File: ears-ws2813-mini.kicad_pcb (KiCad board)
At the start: 2 copper layers, 113 x 153 mm, 204 parts, among them J1 Conn_01x08, J2 Conn_01x02, J3 Conn_01x02, J4 Conn_01x02, J5 Conn_01x02

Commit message: Hopefully this will be revision 2.0
Signed-off-by: Aaron Williams <aaron.w2@gmail.com>
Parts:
- added C100: 4.7nF, Capacitor_SMD:C_0603_1608Metric, F.Cu at (62.4, 185.8)
- added C101: 4.7nF DNI, Capacitor_SMD:C_0603_1608Metric, F.Cu at (69.9, 168.2)
- added C102: 4.7nF DNI, Capacitor_SMD:C_0603_1608Metric, F.Cu at (35.5, 167.0)
- added C99: 4.7nF, Capacitor_SMD:C_0603_1608Metric, F.Cu at (64.0, 185.8)
- C10, C11, C12, C13, C14, C15, C16, C17, C18, C19, C20, C21, C22, C23, C24, C25, C26, C27, C28, C29, C3, C30, C31, C32, C33, C34, C35, C36, C37, C38, C39, C4, C40, C41, C42, C43, C44, C45, C46, C47, C48, C49, C5, C50, C51, C52, C53, C54, C55, C56, C57, C58, C59, C6, C60, C61, C62, C63, C64, C65, C66, C67, C68, C69, C7, C70, C71, C72, C73, C74, C75, C76, C77, C78, C79, C8, C80, C81, C82, C83, C84, C85, C86, C87, C88, C89, C9, C90, C91, C92, C93, C94, C95, C96, C97, C98: value 1uF -> 1uF 25V
- D1, D10, D11, D12, D13, D14, D15, D16, D17, D18, D19, D2, D20, D21, D22, D23, D24, D25, D26, D27, D28, D29, D3, D30, D31, D32, D33, D34, D35, D36, D37, D38, D39, D4, D40, D41, D42, D43, D44, D45, D46, D47, D48, D49, D5, D50, D51, D52, D53, D54, D55, D56, D57, D58, D59, D6, D60, D61, D62, D63, D64, D65, D66, D67, D68, D69, D7, D70, D71, D72, D73, D74, D75, D76, D77, D78, D79, D8, D80, D81, D82, D83, D84, D85, D86, D87, D88, D89, D9, D90, D91, D92, D93, D94, D95, D96: footprint LED_WS2813-mini:LED_WS2813-MINI -> LED_WS2813-mini:LED_WS2813-MINI-2
- moved R2 39.3 mm to (28.5, 167.0), turned to 0 degrees
- moved R1 18.5 mm to (63.4, 168.1), turned to 0 degrees
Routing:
- net Net-(C100-Pad1): track 5.99 -> 73.0 mm, vias 0 -> 3
- net /DIN: track 75.6 -> 15.5 mm
- net Net-(C101-Pad1): track 3.21 -> 29.4 mm
- net /DINB: track 73.3 -> 49.1 mm, vias 0 -> 1
- net GND: track 236.7 -> 253.0 mm, vias 193 -> 196
- net +5V: track 262.4 -> 269.4 mm, vias 21 -> 19
- net /Ears-top and bypass/DOUT7: track 73.1 -> 78.6 mm
- net /Ears-top and bypass/DOUT6: track 80.5 -> 85.4 mm
- net /DOUT1: track 123.2 -> 128.0 mm, vias 4 -> 5
- net /DOUT4: track 102.8 -> 107.3 mm
- net Net-(D50-Pad3): track 13.5 -> 17.1 mm, vias 4 -> 2
- net /DOUT2: track 115.7 -> 119.2 mm, vias 4 -> 5
- net Net-(D82-Pad3): track 13.8 -> 17.2 mm, vias 4 -> 2
- net /DOUT3: track 109.2 -> 112.4 mm, vias 4 -> 5
- net Net-(D37-Pad3): track 14.2 -> 17.4 mm, vias 4 -> 2
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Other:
- board text added: "+ + - -"
- board text added: "+5 GND"
- board text added: "Copyright © 2019 by Aaron Williams"
- board text added: "DIB DI DO DOB"
- board text added: "DIB DI DO DOB 5 5 G G"
- board text added: "DO DOB"
- board text added: "DOB DO"
- board text added: "Revision 2.0"

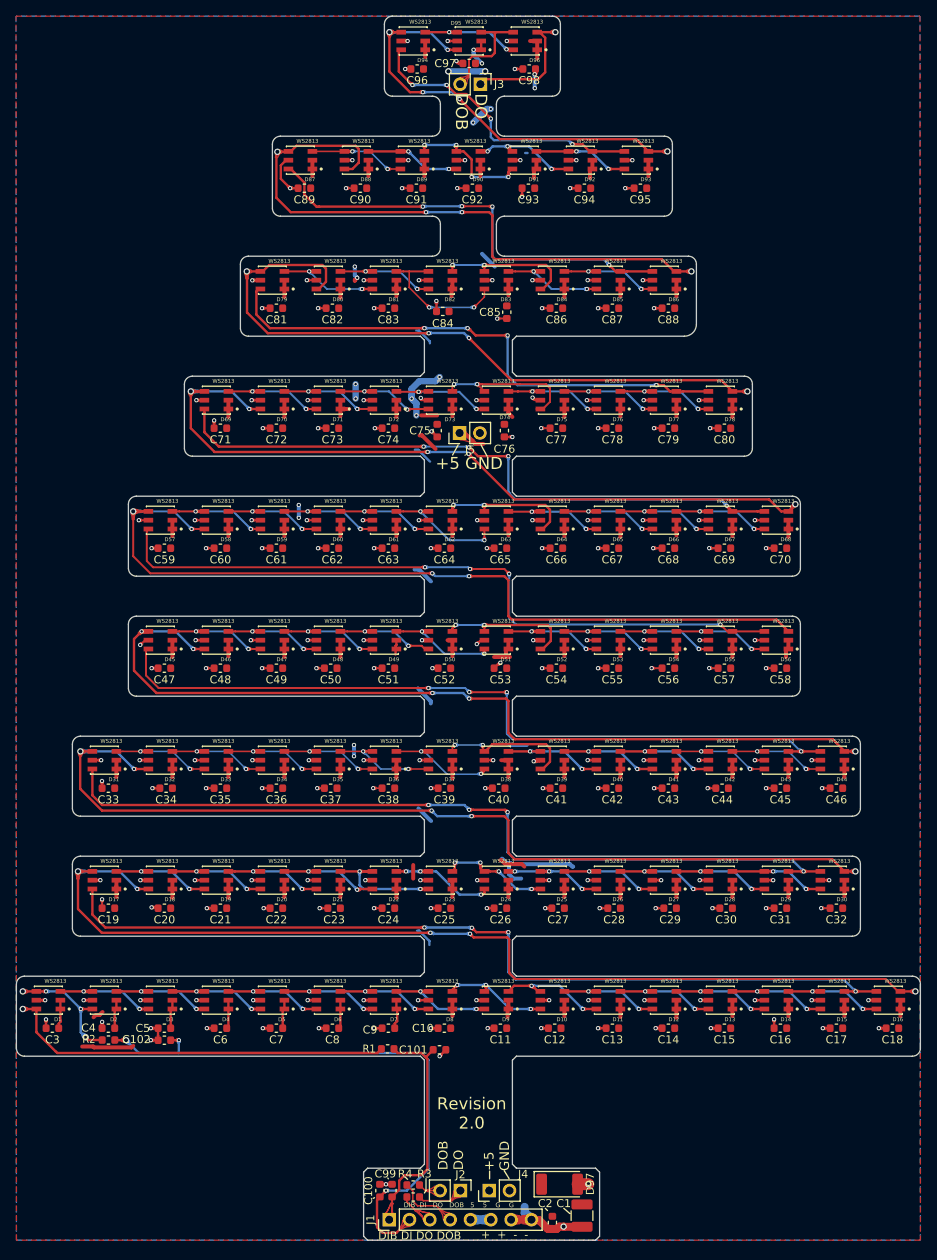
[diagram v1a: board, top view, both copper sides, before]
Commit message: Changing via size from 0.3 to 0.35mm
Signed-off-by: Aaron Williams <aaron.w2@gmail.com>
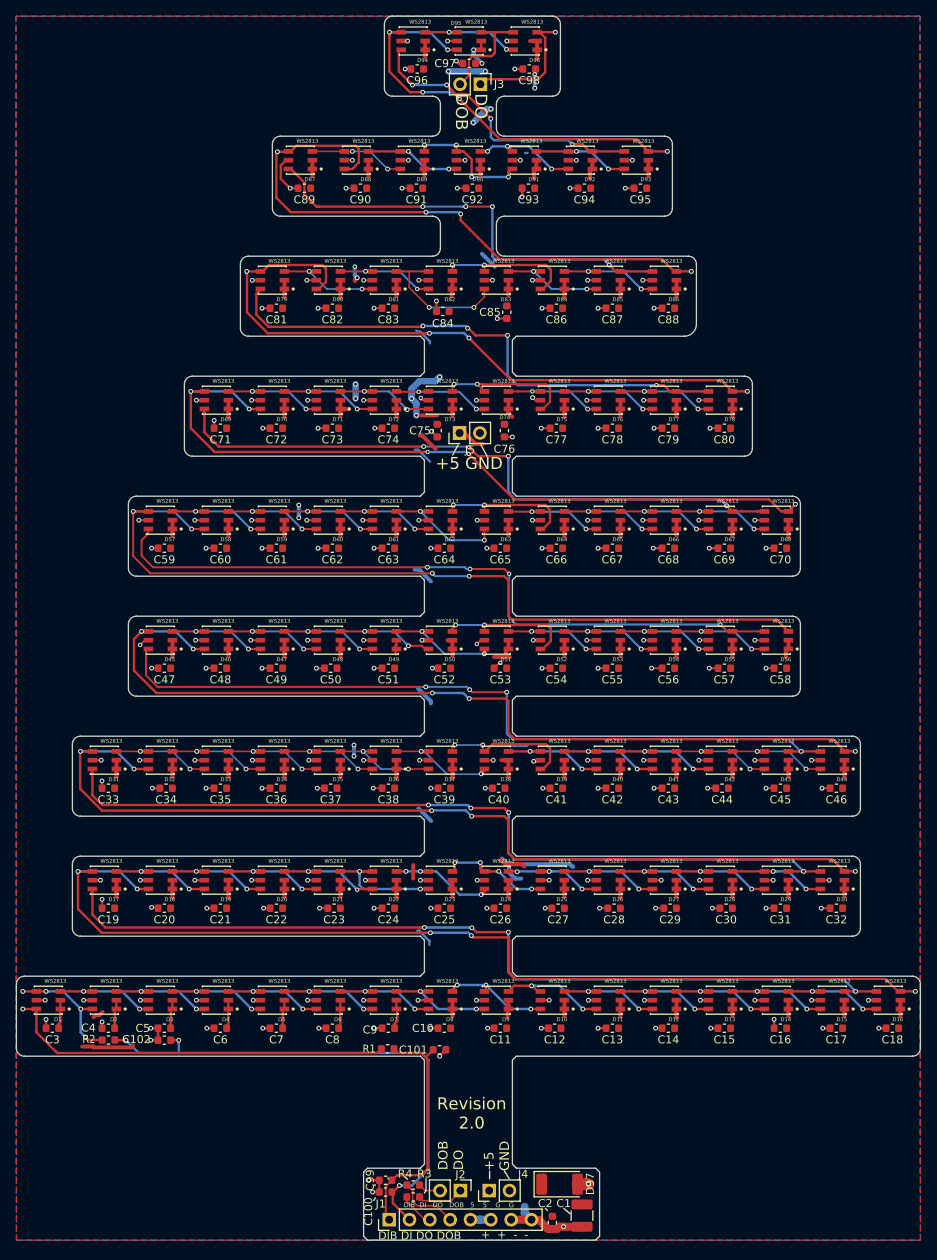
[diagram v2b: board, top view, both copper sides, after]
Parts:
- moved C99 1.53 mm to (63.1, 184.5), turned to 180 degrees
- moved C100 0.73 mm to (63.1, 186.0), turned to 180 degrees
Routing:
- net Net-(C100-Pad1): track 73.0 -> 66.5 mm
- net /Ears-top and bypass/DOUT7: track 78.6 -> 76.1 mm
- net GND: track 253.0 -> 254.9 mm, vias 196 -> 197
- net Net-(C101-Pad1): track 29.4 -> 30.2 mm
- net /DOUTB4: track 87.8 -> 88.4 mm

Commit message: Added more ESD protection and moved a few components.
Version 2.0

Signed-off-by: Aaron Williams <aaron.w2@gmail.com>
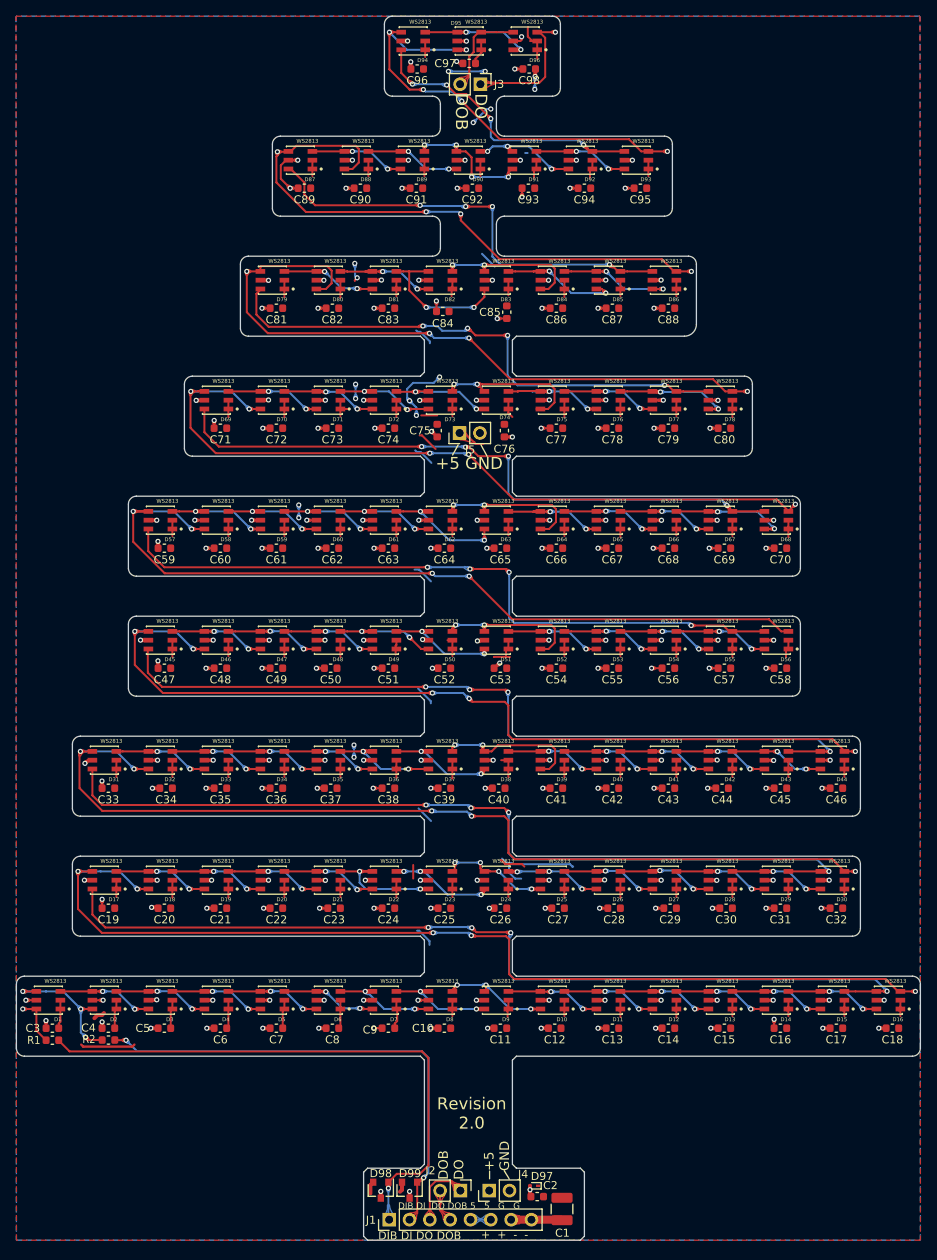
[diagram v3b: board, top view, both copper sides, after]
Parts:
- removed C100, C99: 4.7nF, Capacitor_SMD:C_0603_1608Metric
- removed C101, C102: 4.7nF DNI, Capacitor_SMD:C_0603_1608Metric
- removed R3, R4: 22, Resistor_SMD:R_0603_1608Metric
- added D98: CM1213A-01SO, Package_TO_SOT_SMD:SOT-23, F.Cu at (62.5, 185.8)
- added D99: CM1213A-01SO, Package_TO_SOT_SMD:SOT-23, F.Cu at (66.2, 185.8)
- D97: value D_Schottky -> ESD9101P2T5G; footprint Diode_SMD:D_2010_5025Metric -> Diodes_GIT:D_SOD-923
- moved R1 41.9 mm to (21.5, 167.0)
- moved C2 3.76 mm to (82.1, 186.6), turned to 180 degrees
- moved D97 3.21 mm to (81.7, 185.2), turned to 180 degrees
- moved C1 2.63 mm to (85.2, 188.1)
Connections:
- net Net-(C100-Pad1) renamed /DIN_C
- net Net-(C101-Pad1) renamed /DINB_C
- J1 pad 3: Net-(J1-Pad3) -> /DOUT
- J1 pad 4: Net-(J1-Pad4) -> /DOUTB
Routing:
- net /DINB: track 49.1 -> 6.10 mm
- net /DINB_C: track 30.2 -> 71.3 mm, vias 0 -> 1
- net GND: track 254.9 -> 243.4 mm, vias 197 -> 195
- net Net-(J1-Pad4): track 7.95 -> 0.00 mm
- net +5V: track 269.4 -> 275.4 mm, vias 19 -> 17
- net /DOUTB1: track 109.4 -> 115.1 mm
- net /DOUTB2: track 103.1 -> 108.3 mm
- net /DIN_C: track 66.5 -> 61.5 mm, vias 3 -> 2
- net /DOUTB3: track 96.2 -> 100.8 mm
- net Net-(J1-Pad3): track 4.43 -> 0.00 mm
- net /DOUT4: track 107.3 -> 103.6 mm
- net /DOUT: track 5.93 -> 8.88 mm
- net Net-(D83-Pad3): track 12.8 -> 15.6 mm
- net Net-(D51-Pad3): track 14.1 -> 11.9 mm
- net /Ears-top and bypass/DOUTB: track 13.9 -> 11.7 mm
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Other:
- outline, holes or cut-outs redrawn
- net class Default: via_dia 0.54 -> 0.65; via_drill 0.3 -> 0.35
- rule via_min_size: 0.54 -> 0.65
